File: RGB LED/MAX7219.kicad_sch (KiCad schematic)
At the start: 2 parts, among them U2 MAX7219

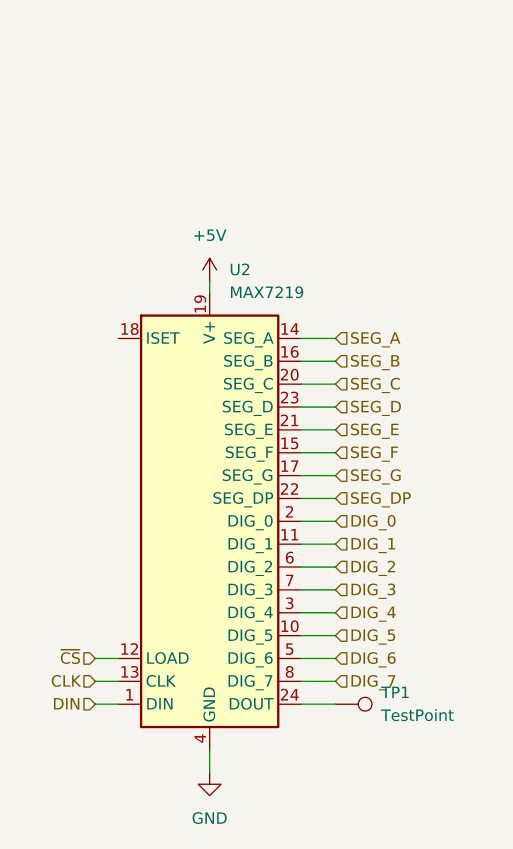
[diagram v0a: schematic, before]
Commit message: edited according to feedback
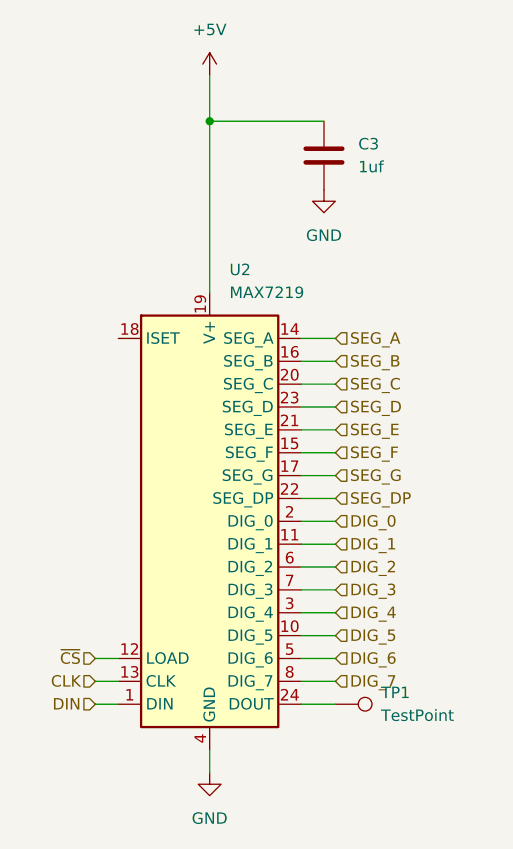
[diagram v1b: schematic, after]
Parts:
- added C3: 1uf, symbol Device:C
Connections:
- net +5V: now also C3.1
- net GND: now also C3.2
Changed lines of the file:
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@@
 (kicad_sch (version 20230121) (generator eeschema)
   (paper "A4")
-  (wire (pts (xy 92.71 59.69) (xy 92.71 60.96))
+  (junction (at 92.71 41.91) (diameter 0) (color 0 0 0 0)
+  )
+  (wire (pts (xy 92.71 36.83) (xy 92.71 41.91))
     (stroke (width 0) (type default))
   )
@@
     (stroke (width 0) (type default))
   )
+  (wire (pts (xy 92.71 41.91) (xy 92.71 60.96))
+    (stroke (width 0) (type default))
+  )
   (wire (pts (xy 102.87 106.68) (xy 106.68 106.68))
     (stroke (width 0) (type default))
@@
   )
   (wire (pts (xy 102.87 83.82) (xy 106.68 83.82))
+    (stroke (width 0) (type default))
+  )
+  (wire (pts (xy 92.71 41.91) (xy 105.41 41.91))
     (stroke (width 0) (type default))
   )
@@
     )
   )
-  (symbol (lib_id "power:+5V") (at 92.71 59.69 0) (unit 1)
-    (in_bom yes) (on_board yes) (dnp no) (fields_autoplaced)
-    (property "Reference" "#PWR06" (at 92.71 63.5 0)
-      (effects (font (size 1.27 1.27)) hide)
-    )
-    (property "Value" "+5V" (at 92.71 54.61 0)
+  (symbol (lib_id "power:+5V") (at 92.71 36.83 0) (unit 1)
+    (in_bom yes) (on_board yes) (dnp no) (fields_autoplaced)
+    (property "Reference" "#PWR06" (at 92.71 40.64 0)
+      (effects (font (size 1.27 1.27)) hide)
+    )
+    (property "Value" "+5V" (at 92.71 31.75 0)
       (effects (font (size 1.27 1.27)))
     )
-    (property "Footprint" "" (at 92.71 59.69 0)
-      (effects (font (size 1.27 1.27)) hide)
-    )
-    (property "Datasheet" "" (at 92.71 59.69 0)
+    (property "Footprint" "" (at 92.71 36.83 0)
+      (effects (font (size 1.27 1.27)) hide)
+    )
+    (property "Datasheet" "" (at 92.71 36.83 0)
       (effects (font (size 1.27 1.27)) hide)
     )
@@
     )
   )
+  (symbol (lib_id "power:GND") (at 105.41 49.53 0) (unit 1)
+    (in_bom yes) (on_board yes) (dnp no) (fields_autoplaced)
+    (property "Reference" "#PWR017" (at 105.41 55.88 0)
+      (effects (font (size 1.27 1.27)) hide)
+    )
+    (property "Value" "GND" (at 105.41 54.61 0)
+      (effects (font (size 1.27 1.27)))
+    )
+    (property "Footprint" "" (at 105.41 49.53 0)
+      (effects (font (size 1.27 1.27)) hide)
+    )
+    (property "Datasheet" "" (at 105.41 49.53 0)
+      (effects (font (size 1.27 1.27)) hide)
+    )
+    (pin "1")
+    (instances
+      (project "RGB LED"
+        (path "/ac9a3c3e-b738-422c-8f43-94adc2643155/af166803-f831-47e1-93fe-64e366332d2a"
+          (reference "#PWR017") (unit 1)
+        )
+      )
+    )
+  )
   (symbol (lib_id "Connector:TestPoint") (at 106.68 106.68 270) (unit 1)
     (in_bom yes) (on_board yes) (dnp no) (fields_autoplaced)
@@
         )
       )
+    )
+  )
+  (symbol (lib_id "Device:C") (at 105.41 45.72 0) (unit 1)
+    (in_bom yes) (on_board yes) (dnp no) (fields_autoplaced)
+    (property "Reference" "C3" (at 109.22 44.45 0)
+      (effects (font (size 1.27 1.27)) (justify left))
+    )
+    (property "Value" "1uf" (at 109.22 46.99 0)
+      (effects (font (size 1.27 1.27)) (justify left))
+    )
+    (property "Footprint" "" (at 106.3752 49.53 0)
+      (effects (font (size 1.27 1.27)) hide)
+    )
+    (property "Datasheet" "~" (at 105.41 45.72 0)
+      (effects (font (size 1.27 1.27)) hide)
+    )
+    (pin "1")
+    (pin "2")
+    (instances
+      (project "RGB LED"
+        (path "/ac9a3c3e-b738-422c-8f43-94adc2643155/af166803-f831-47e1-93fe-64e366332d2a"
+          (reference "C3") (unit 1)
+        )
+      )

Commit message: added footprints
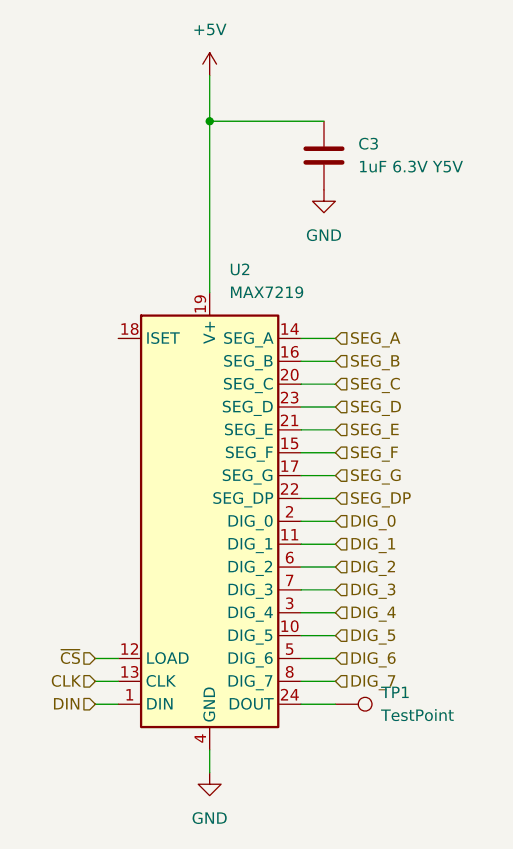
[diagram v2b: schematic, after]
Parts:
- C3: value 1uf -> 1uF 6.3V Y5V; footprint (none) -> Capacitor_SMD:C_0603_1608Metric
- TP1: footprint (none) -> TestPoint:TestPoint_Keystone_5015_Micro-Minature
- U2: footprint (none) -> Package_SO:SOP-24_7.5x15.4mm_P1.27mm
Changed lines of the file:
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@@
       (effects (font (size 1.27 1.27)) (justify left))
     )
-    (property "Footprint" "" (at 91.44 85.09 0)
+    (property "Footprint" "Package_SO:SOP-24_7.5x15.4mm_P1.27mm" (at 91.44 85.09 0)
       (effects (font (size 1.27 1.27)) hide)
     )
-    (property "Datasheet" "https://datasheets.maximintegrated.com/en/ds/MAX7219-MAX7221.pdf" (at 93.98 90.17 0)
+    (property "Datasheet" "https://datasheet.lcsc.com/lcsc/2305251403_HGSEMI-MAX7219M-TR_C6705351.pdf" (at 93.98 90.17 0)
       (effects (font (size 1.27 1.27)) hide)
     )
@@
       (effects (font (size 1.27 1.27)) (justify left))
     )
-    (property "Footprint" "" (at 106.68 111.76 0)
+    (property "Footprint" "TestPoint:TestPoint_Keystone_5015_Micro-Minature" (at 106.68 111.76 0)
       (effects (font (size 1.27 1.27)) hide)
     )
-    (property "Datasheet" "~" (at 106.68 111.76 0)
+    (property "Datasheet" "https://www.koaspeer.com/pdfs/RC.pdf" (at 106.68 111.76 0)
       (effects (font (size 1.27 1.27)) hide)
     )
@@
       (effects (font (size 1.27 1.27)) (justify left))
     )
-    (property "Value" "1uf" (at 109.22 46.99 0)
+    (property "Value" "1uF 6.3V Y5V" (at 109.22 46.99 0)
       (effects (font (size 1.27 1.27)) (justify left))
     )
-    (property "Footprint" "" (at 106.3752 49.53 0)
+    (property "Footprint" "Capacitor_SMD:C_0603_1608Metric" (at 106.3752 49.53 0)
       (effects (font (size 1.27 1.27)) hide)
     )

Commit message: schematic edits
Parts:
- added R4: 10K, Resistor_SMD:R_0603_1608Metric, symbol Device:R
- TP1: value TestPoint -> RCWTE
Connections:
- net +5V: now also R4.1
- net at U2.18 (ISET): now also R4.2
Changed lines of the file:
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@@
 (kicad_sch (version 20230121) (generator eeschema)
   (paper "A4")
+  (junction (at 92.71 57.15) (diameter 0) (color 0 0 0 0)
+  )
   (junction (at 92.71 41.91) (diameter 0) (color 0 0 0 0)
   )
@@
     (stroke (width 0) (type default))
   )
+  (wire (pts (xy 78.74 64.77) (xy 78.74 66.04))
+    (stroke (width 0) (type default))
+  )
   (wire (pts (xy 102.87 68.58) (xy 106.68 68.58))
     (stroke (width 0) (type default))
@@
     (stroke (width 0) (type default))
   )
+  (wire (pts (xy 92.71 57.15) (xy 92.71 60.96))
+    (stroke (width 0) (type default))
+  )
   (wire (pts (xy 102.87 76.2) (xy 106.68 76.2))
     (stroke (width 0) (type default))
@@
     (stroke (width 0) (type default))
   )
-  (wire (pts (xy 92.71 41.91) (xy 92.71 60.96))
+  (wire (pts (xy 92.71 41.91) (xy 92.71 57.15))
+    (stroke (width 0) (type default))
+  )
+  (wire (pts (xy 78.74 57.15) (xy 92.71 57.15))
     (stroke (width 0) (type default))
   )
@@
   )
   (wire (pts (xy 102.87 91.44) (xy 106.68 91.44))
+    (stroke (width 0) (type default))
+  )
+  (wire (pts (xy 78.74 66.04) (xy 82.55 66.04))
     (stroke (width 0) (type default))
   )
@@
     )
   )
+  (symbol (lib_id "Device:R") (at 78.74 60.96 0) (unit 1)
+    (in_bom yes) (on_board yes) (dnp no) (fields_autoplaced)
+    (property "Reference" "R4" (at 81.28 59.69 0)
+      (effects (font (size 1.27 1.27)) (justify left))
+    )
+    (property "Value" "10K" (at 81.28 62.23 0)
+      (effects (font (size 1.27 1.27)) (justify left))
+    )
+    (property "Footprint" "Resistor_SMD:R_0603_1608Metric" (at 76.962 60.96 90)
+      (effects (font (size 1.27 1.27)) hide)
+    )
+    (property "Datasheet" "~" (at 78.74 60.96 0)
+      (effects (font (size 1.27 1.27)) hide)
+    )
+    (pin "2")
+    (pin "1")
+    (instances
+      (project "RGB LED"
+        (path "/ac9a3c3e-b738-422c-8f43-94adc2643155/af166803-f831-47e1-93fe-64e366332d2a"
+          (reference "R4") (unit 1)
+        )
+      )
+    )
+  )
   (symbol (lib_id "Connector:TestPoint") (at 106.68 106.68 270) (unit 1)
     (in_bom yes) (on_board yes) (dnp no) (fields_autoplaced)
@@
       (effects (font (size 1.27 1.27)) (justify left))
     )
-    (property "Value" "TestPoint" (at 111.76 107.95 90)
-      (effects (font (size 1.27 1.27)) (justify left))
-    )
+    (property "Value" "RCWTE" (at 111.76 107.95 90)
+      (effects (font (size 1.27 1.27)) (justify left))
+    )
